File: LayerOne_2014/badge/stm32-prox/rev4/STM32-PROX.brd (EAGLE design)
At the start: 85.6 x 49.4 mm, 277 parts, among them IC10 74XX244, IC105 MCP1824T-250, IC106 MCP1824T-120, IC11 CD4066, IC13 PQ1X331M2ZP-3V3-LDO-SOT-23-5, IC14 AD8052, IC2 STM32F1_HIGH_DENSITY_LQFP64LQ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, IC3 PQ1X331M2ZP-3V3-LDO-SOT-23-5, IC4 HCU-INVERTER, IC5 TLV3502, IC6 MCP6294, IC7 MCP100, IC8 TLC5540, IC9 74XX244, Q1 NPN-SOT23-2N3904, Q2 BC817-16SMD, Q3 MMBT2222, Q4 BC817-16SMD, U1 FERRITE0805, U2 XC3S50, U3 UG-2864HSWEG01, U4 SDCARD, Y1 8Mhz

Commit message: VDD / 5V Fix
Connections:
- removed net VDD: C21.1, C22.1, C23.1, C24.1, C37.+, C38.+, C44.1, C46.1, C71.1, C72.1, C73.+, D7.3, FB1.2, FB2\.2, FB3.2, IC10.20, IC105.1, IC106.1, IC11.14, IC13.1, IC14.8, IC3.1, IC3.3, IC5.8, IC6.4, IC8.11, IC8.13, IC9.20, R47.1, R52.2, R9.2, RLY1.1
- net 5V: now also C21.1, C22.1, C23.1, C24.1, C37.+, C38.+, C44.1, C46.1, C71.1, C72.1, C73.+, D7.3, FB1.2, FB2\.2, FB3.2, IC10.20, IC105.1, IC106.1, IC11.14, IC13.1, IC14.8, IC3.1, IC3.3, IC5.8, IC6.4, IC8.11, IC8.13, IC9.20, R47.1, R52.2, R9.2, RLY1.1
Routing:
- net 5V: track 15.7 -> 202.5 mm, vias 1 -> 10
- net VDD: track 186.8 -> 0.00 mm, vias 9 -> 0

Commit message: larger board.
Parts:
- C4, C5, C6, C7, C8: device STM32-PROX:0603-CAP -> STM32-PROX:RLC_0603
- C58, C59, C60, C61, C62, C63, C64: device STM32-PROX:SPARKFUN_0603-CAP -> STM32-PROX:RLC_0603
- FB1, FB2\, FB3, R1, R10, R102, R11, R12, R13, R14, R15, R16, R17, R18, R19, R2, R20, R21, R22, R23, R24, R25, R26, R27, R28, R29, R3, R30, R31, R319, R32, R33, R34, R35, R36, R37, R38, R39, R4, R40, R41, R42, R43, R44, R45, R46, R47, R48, R49, R5, R50, R51, R52, R53, R54, R55, R56, R57, R58, R59, R6, R60, R61, R62, R63, R64, R65, R66, R67, R68, R69, R7, R70, R71, R8, R9: device STM32-PROX:RLC_0603 -> STM32-PROX:RLC_0603@1
- moved C70 1.67 mm to (36.7, 34.9)
- moved C65 1.27 mm to (38.7, 33.9)
- moved R102 1.27 mm to (32.8, 32.4)
- moved R23 1.27 mm to (34.7, 32.4)
- moved R54 1.14 mm to (40.4, 33.9)
- moved C18 1.02 mm to (42.0, 33.9)
- moved R53 0.89 mm to (43.7, 33.9)
- moved C71 0.76 mm to (44.2, 40.8)
- moved TP8 0.76 mm to (78.2, 32.0)
- moved C35 0.68 mm to (11.3, 24.4)
- moved R319 0.63 mm to (58.5, 27.6)
- moved C19 0.51 mm to (45.5, 33.9)
- moved C58 0.46 mm to (73.9, 41.1)
- moved C36 0.40 mm to (10.9, 22.5)
- moved C44 0.38 mm to (45.8, 40.8)
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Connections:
- net 5V renamed VDD
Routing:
- net VDD: track 202.5 -> 232.5 mm, vias 10 -> 13
- net GND: track 53.3 -> 57.9 mm, vias 107 -> 115
- net N$39: track 13.4 -> 16.1 mm
- net AMPL_LO: track 58.6 -> 60.9 mm
- net FPGA_ON: track 53.5 -> 55.1 mm
- net +2V5: track 83.1 -> 84.5 mm
- net N$55: track 10.9 -> 12.0 mm
- net N$48: track 6.54 -> 7.19 mm
- net SPEAKER: track 10.3 -> 9.69 mm
- net ANT_HI: track 17.2 -> 17.8 mm
- net +3V3: track 224.3 -> 224.8 mm

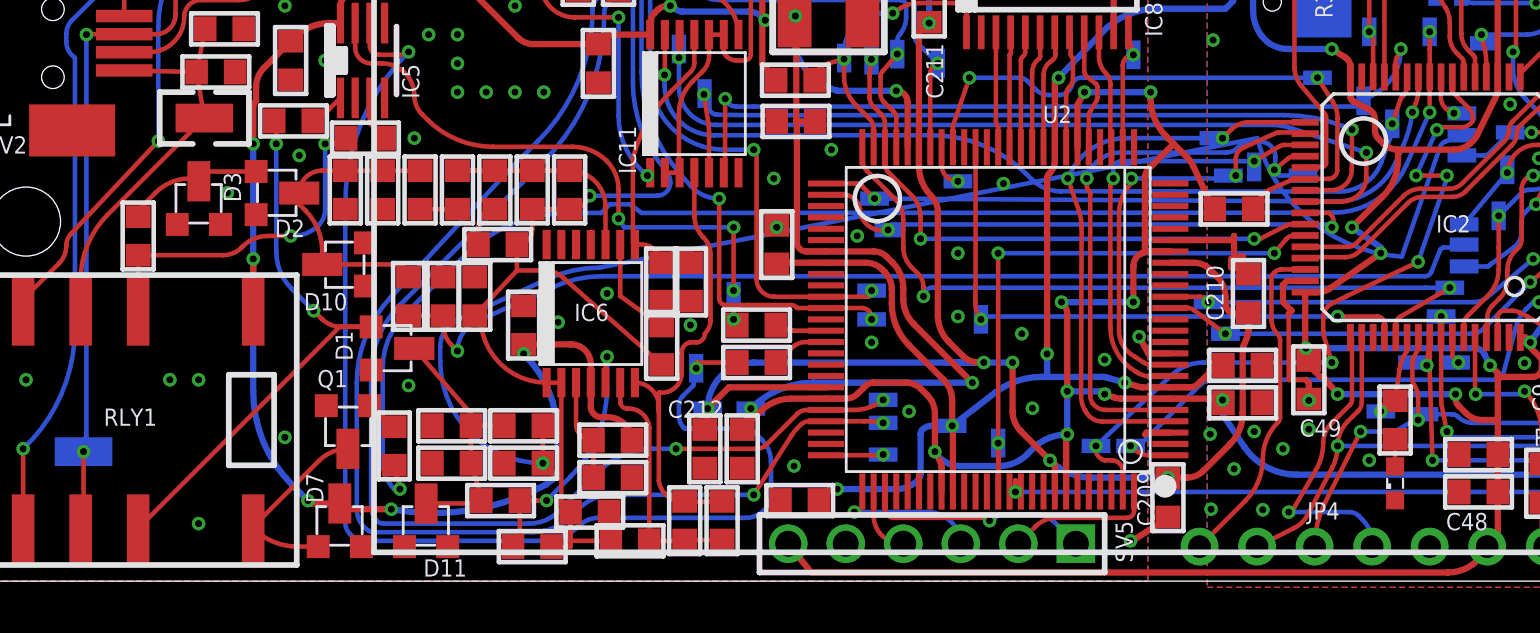
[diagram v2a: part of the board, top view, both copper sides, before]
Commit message: moved D1 fixed trace overlap again renamed oled miso sdin to sdout
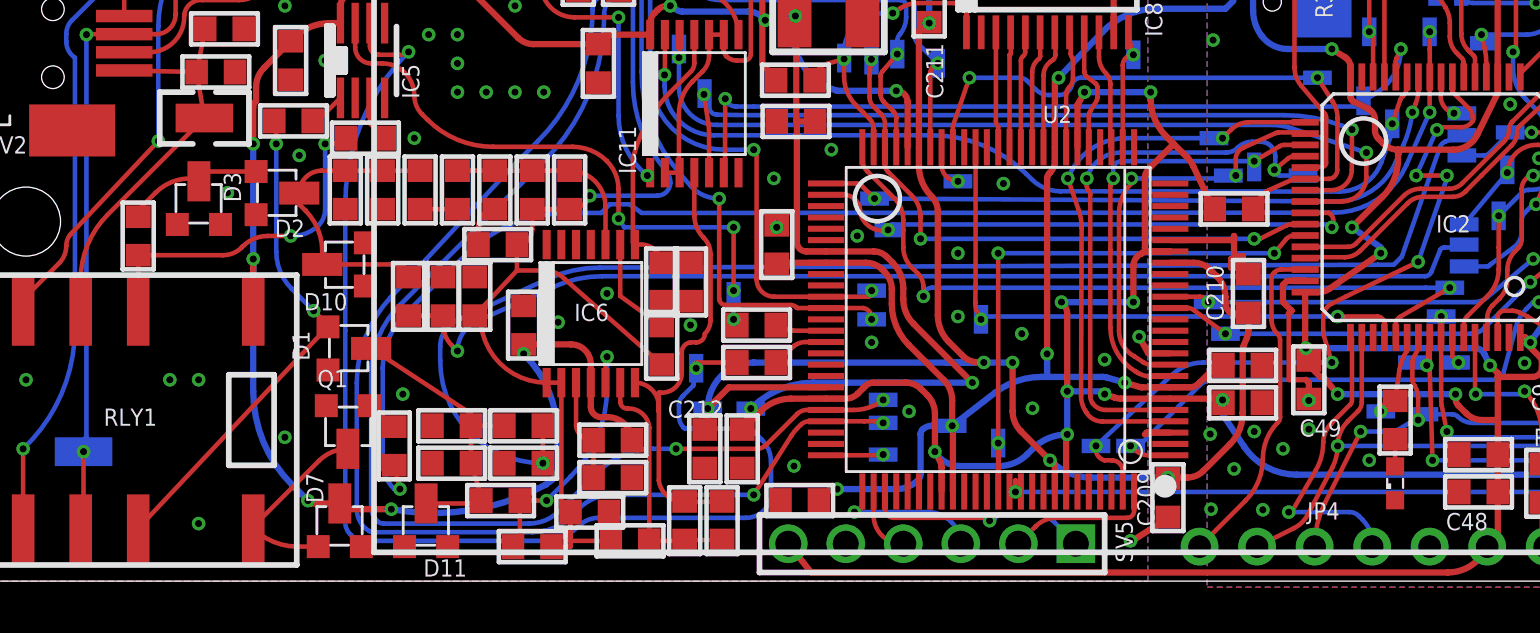
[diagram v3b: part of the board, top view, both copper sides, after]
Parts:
- moved D1 1.91 mm to (16.6, 10.3)
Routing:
- net B_RLY_NC: track 25.7 -> 22.2 mm
- net AMPL_LO: track 60.9 -> 58.6 mm
- net N$19: track 11.7 -> 13.2 mm

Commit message: 
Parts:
- added C76: 100nF, STM32-PROX:RLC_0603
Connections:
- net N$67: now also C76.2
- net VBAT+: now also C76.1
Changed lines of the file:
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@@
 <attribute name="DIGIKEY" value="311-820KGRTR-ND" x="63.5" y="29.21" size="1.778" layer="27" rot="R90" display="off"/>
 </element>
+<element name="C76" library="STM32-PROX" package="RLC_0603" value="100nF" x="1.27" y="-2.54">
+<attribute name="OC_NEWARK" value="85K9474" x="1.27" y="-2.54" size="1.778" layer="27" display="off"/>
+<attribute name="PARTNO" value="CL10B104KO8NNNC" x="1.27" y="-2.54" size="1.778" layer="27" display="off"/>
+<attribute name="MPN" value="CL10B104KO8NNNC" x="1.27" y="-2.54" size="1.778" layer="27" display="off"/>
+<attribute name="MF" value="" x="1.27" y="-2.54" size="1.778" layer="27" display="off"/>
+<attribute name="DIGIKEY" value="1276-1005-1-ND" x="1.27" y="-2.54" size="1.778" layer="27" display="off"/>
+</element>
 </elements>
 <signals>
@@
 <wire x1="81.230621875" y1="33.097621875" x2="81.165865625" y2="33.0708" width="0.2794" layer="1" curve="-45"/>
 <wire x1="81.165865625" y1="33.0708" x2="80.01" y2="33.0708" width="0.2794" layer="1"/>
+<contactref element="C76" pad="1"/>
+<wire x1="0.42" y1="-2.54" x2="76.327" y2="26.035" width="0" layer="19" extent="1-1"/>
 </signal>
 <signal name="N$64">
@@
 <wire x1="74.676" y1="36.156" x2="75.653" y2="35.179" width="0.2032" layer="1" curve="90"/>
 <wire x1="75.653" y1="35.179" x2="75.692" y2="35.521" width="0.2032" layer="1"/>
+<contactref element="C76" pad="2"/>
+<wire x1="2.12" y1="-2.54" x2="74.676" y2="36.156" width="0" layer="19" extent="1-1"/>
 </signal>
 <signal name="N$68">
